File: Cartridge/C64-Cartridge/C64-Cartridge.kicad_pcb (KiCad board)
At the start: 2 copper layers, 58 x 35.9 mm, 22 parts, among them J1 C64_Expansion_port, J2 GND, SW1 SW_DIP_x08, SW2 RESET, SW3 RESET, U1 SST39SF040

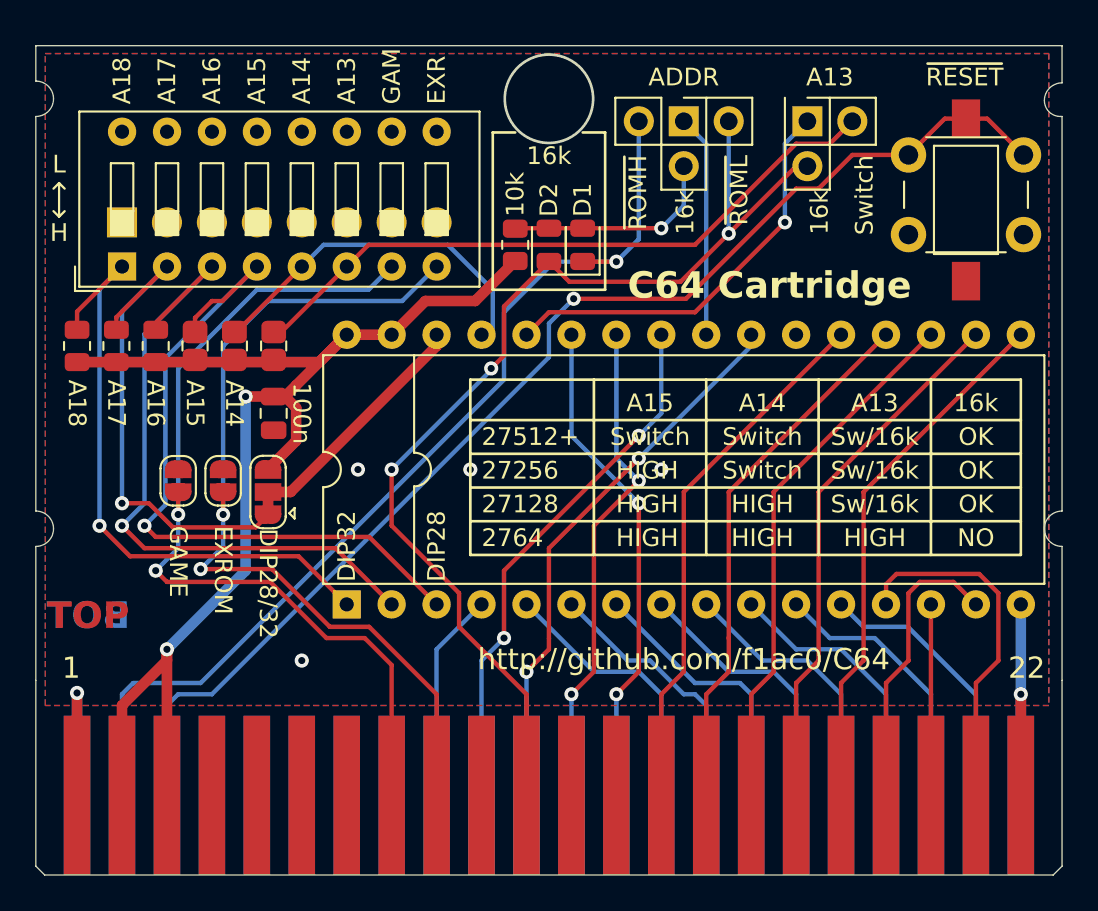
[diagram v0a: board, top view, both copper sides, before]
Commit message: C64-Cartridge : addition of EpyxFastload daughter board ; some silkscreen changes. C64-KungFuFlash, C64-Pi1541 : small updates before production. New C64-efuse board that fit inside the DIN plug.
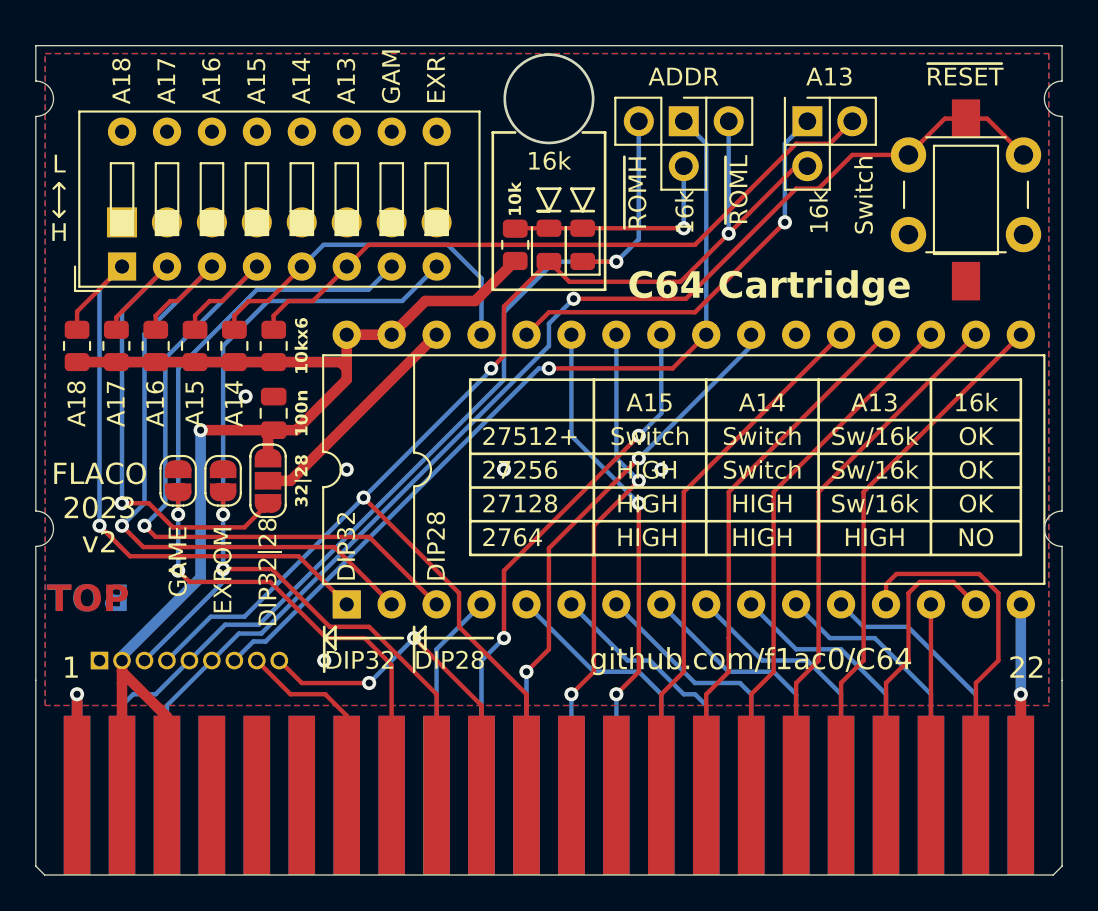
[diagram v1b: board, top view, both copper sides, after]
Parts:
- removed REF**: OSHW-Logo_11.4x12mm_SilkScreen, Symbol:OSHW-Logo_11.4x12mm_SilkScreen
- added FID1: License, Sassa:CC_BY_NC_SA_square_silkscreen, B.Cu at (87.0, 116.8)
- added J3: Epyx FastLoad mod, Connector_PinHeader_1.27mm:PinHeader_1x09_P1.27mm_Vertical, B.Cu at (82.5, 127.0)
- JP3: value 27C512 -> DIP32/28; footprint Jumper:SolderJumper-3_P1.3mm_Bridged12_RoundedPad1.0x1.5mm -> Jumper:SolderJumper-3_P1.3mm_Open_RoundedPad1.0x1.5mm
- R1, R2, R3: footprint Sassa:C_0805_2012Metric_shortable -> Resistor_SMD:R_0805_2012Metric
- moved JP3 0.63 mm to (92.1, 116.8)
- turned C1 to 90 degrees
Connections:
- J1 pad 10: unconnected-(J1-~{I/O2}-Pad10) -> //IO2
- J1 pad 7: unconnected-(J1-~{I/O1}-Pad7) -> //IO1
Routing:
- net //OE: track 12.0 -> 46.3 mm, vias 0 -> 1
- net //IO2: track 0.00 -> 19.7 mm, vias 0 -> 2
- net //ROML: track 61.2 -> 77.4 mm
- net //IO1: track 0.00 -> 10.9 mm
- net //EXROM: track 50.3 -> 55.5 mm
- net +5V: track 73.6 -> 70.8 mm, vias 2 -> 1
- net //GAME: track 50.6 -> 48.8 mm
- net /ADDR_16K: track 12.3 -> 13.0 mm
- net /ROMA17: track 13.6 -> 12.9 mm
- net GND: track 28.2 -> 28.0 mm, vias 6 -> 7
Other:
- outline, holes or cut-outs redrawn
- board text added: "10kx6"
- board text added: "32|28"
- board text added: "DIP32|28"
- board text added: "Epyx FastLoad mod"
- board text added: "github.com/f1ac0/C64"
- board text removed: "DIP28/32"
